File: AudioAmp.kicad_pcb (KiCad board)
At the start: 2 copper layers, 145 x 40 mm, 55 parts, among them J1 ACJS-MHOM, J2 ACJS-MHOM, Q1 MJE182G, Q12 MMBT5401, Q13 MMBT5401, Q2 MJE172G, Q3 MMBT5551(RANGE:200-300), Q9 MMBT5551(RANGE:200-300)

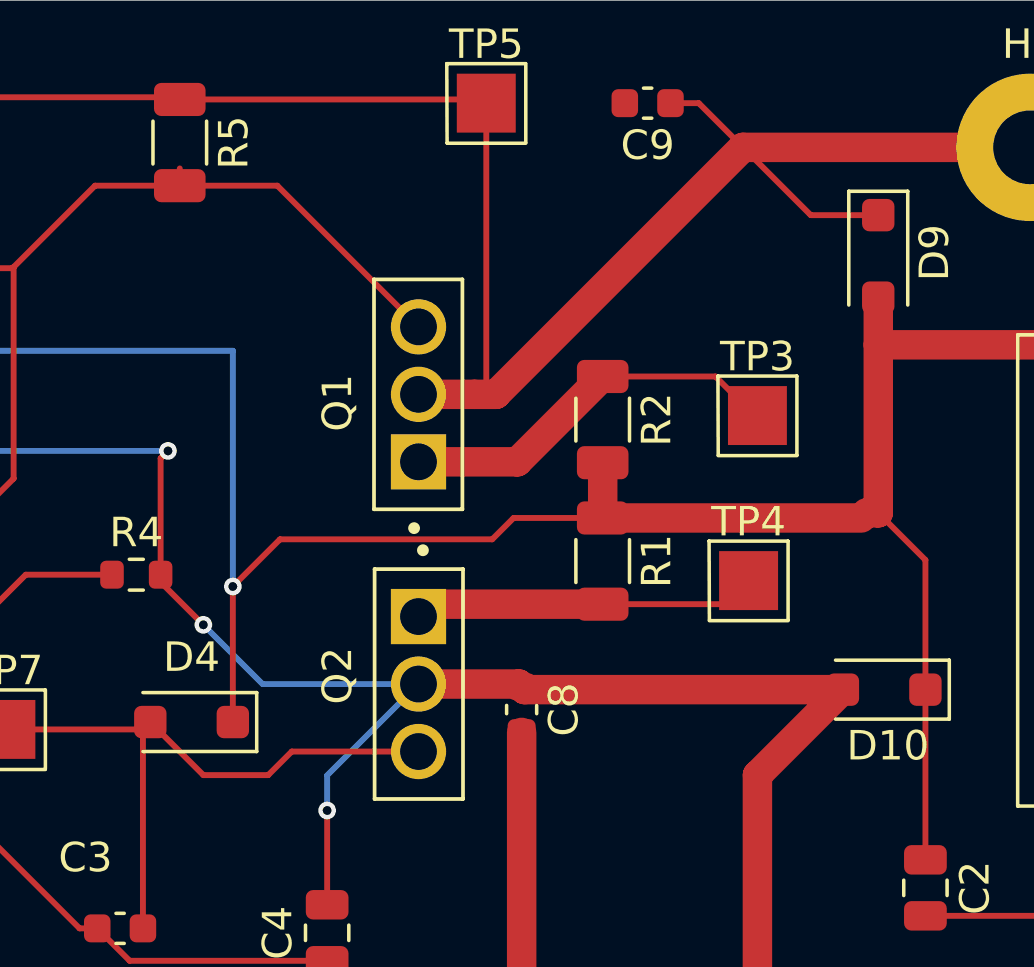
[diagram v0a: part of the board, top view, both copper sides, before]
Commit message: CHA: Insel ohne Füllung gefüllt, dazu via gesetz
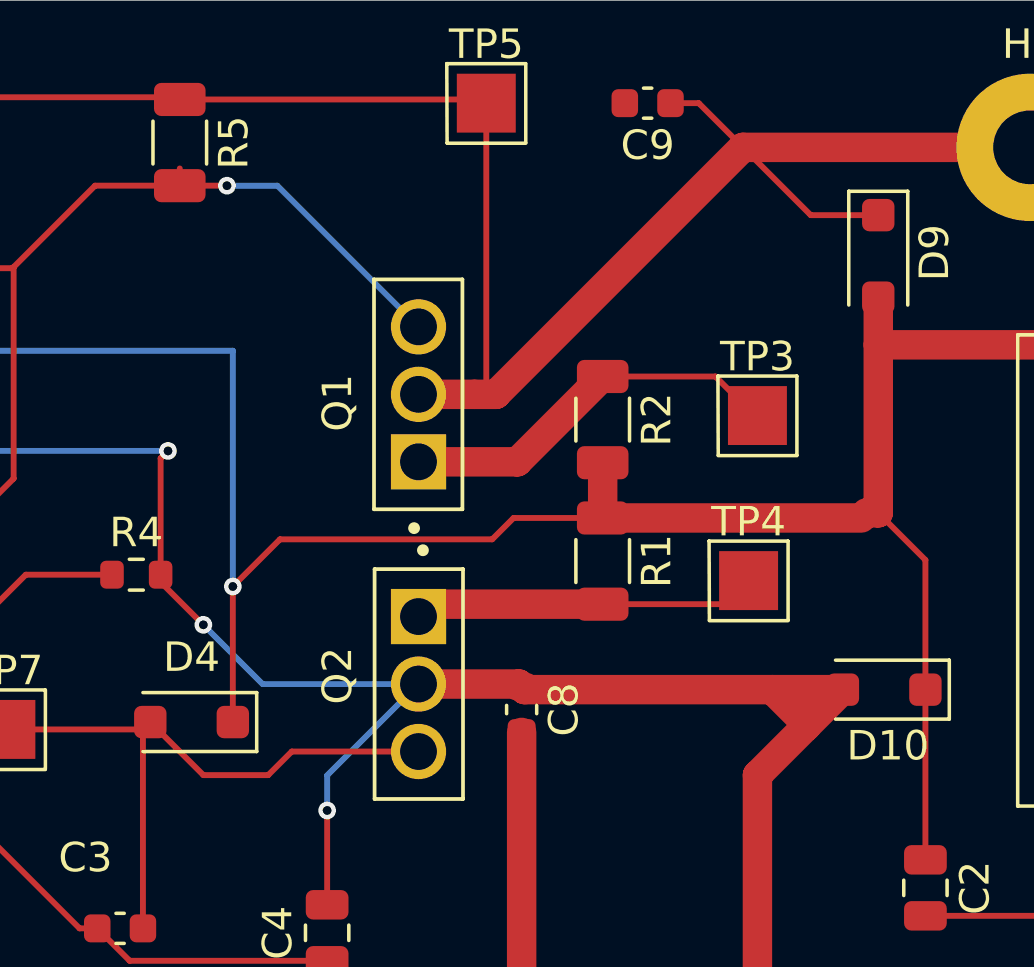
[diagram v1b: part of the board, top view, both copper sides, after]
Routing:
- net Net-(D10-A): track 90.3 -> 92.0 mm
- net Net-(D1-K): vias 0 -> 1
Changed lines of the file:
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@@
 	(segment
 		(start 168.9 110.9)
-		(end 158.1 110.9)
+		(end 166.5 110.9)
 		(width 1)
 		(layer "F.Cu")
@@
 	)
 	(segment
+		(start 166.5 110.9)
+		(end 158.1 110.9)
+		(width 1)
+		(layer "F.Cu")
+		(net 7)
+	)
+	(segment
 		(start 157.91 110.71)
 		(end 158 110.8)
@@
 	(segment
 		(start 166 113.8)
-		(end 168.9 110.9)
+		(end 167.65 112.15)
 		(width 1)
 		(layer "F.Cu")
@@
 	)
 	(segment
+		(start 167.65 112.15)
+		(end 168.9 110.9)
+		(width 1)
+		(layer "F.Cu")
+		(net 7)
+	)
+	(segment
 		(start 124 111.5)
 		(end 120.5 115)
@@
 	)
 	(segment
+		(start 167.65 112.05)
+		(end 166.5 110.9)
+		(width 1)
+		(layer "F.Cu")
+		(net 7)
+	)
+	(segment
 		(start 166.2 122.8)
 		(end 166 123)
@@
 		(start 158.1 110.9)
 		(end 158 110.8)
+		(width 1)
+		(layer "F.Cu")
+		(net 7)
+	)
+	(segment
+		(start 167.65 112.15)
+		(end 167.65 112.05)
 		(width 1)
 		(layer "F.Cu")
@@
 	)
 	(segment
+		(start 146.4 93.8)
+		(end 148 93.8)
+		(width 0.2)
+		(layer "F.Cu")
+		(net 11)
+	)
+	(segment
 		(start 137 107.5)
 		(end 140.7625 103.7375)
@@
 	)
 	(segment
+		(start 140.7625 103.7375)
+		(end 140.7625 96.5625)
+		(width 0.2)
+		(layer "F.Cu")
+		(net 11)
+	)
+	(segment
+		(start 136.9 107.6)
+		(end 137 107.5)
+		(width 0.2)
+		(layer "F.Cu")
+		(net 11)
+	)
+	(segment
+		(start 132 107.6)
+		(end 136.9 107.6)
+		(width 0.2)
+		(layer "F.Cu")
+		(net 11)
+	)
+	(via
+		(at 148 93.8)
+		(size 0.6)
+		(drill 0.3)
+		(layers "F.Cu" "B.Cu")
+		(net 11)
+	)
+	(segment
+		(start 148 93.8)
+		(end 149.71 93.8)
+		(width 0.2)
+		(layer "B.Cu")
+		(net 11)
+	)
+	(segment
 		(start 149.71 93.8)
 		(end 154.5 98.59)
 		(width 0.2)
-		(layer "F.Cu")
-		(net 11)
-	)
-	(segment
-		(start 140.7625 103.7375)
-		(end 140.7625 96.5625)
-		(width 0.2)
-		(layer "F.Cu")
-		(net 11)
-	)
-	(segment
-		(start 136.9 107.6)
-		(end 137 107.5)
-		(width 0.2)
-		(layer "F.Cu")
-		(net 11)
-	)
-	(segment
-		(start 132 107.6)
-		(end 136.9 107.6)
-		(width 0.2)
-		(layer "F.Cu")
-		(net 11)
-	)
-	(segment
-		(start 146.4 93.8)
-		(end 149.71 93.8)
-		(width 0.2)
-		(layer "F.Cu")
-		(net 11)
-	)
+		(layer "B.Cu")
+		(net 11)
+	)

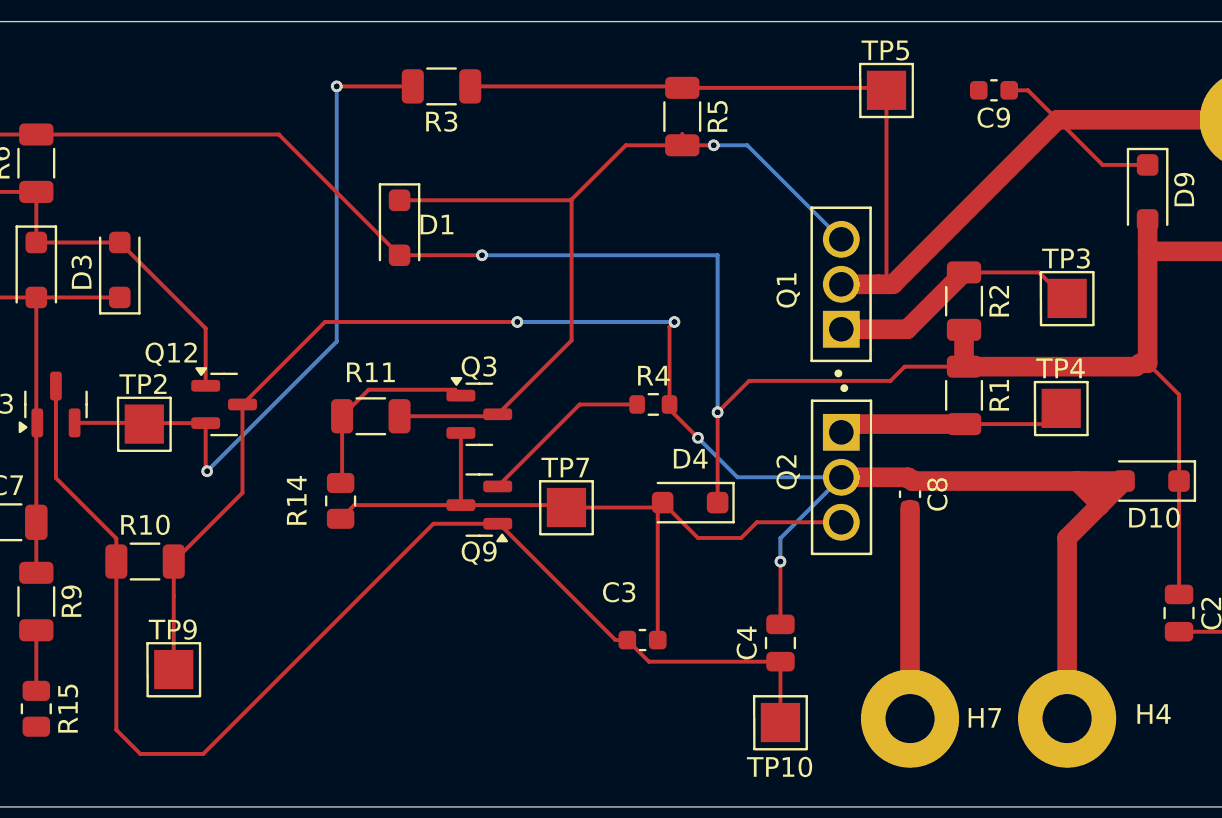
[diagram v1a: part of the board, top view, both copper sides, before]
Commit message: ^CHA: Verbesserungen Füll GND
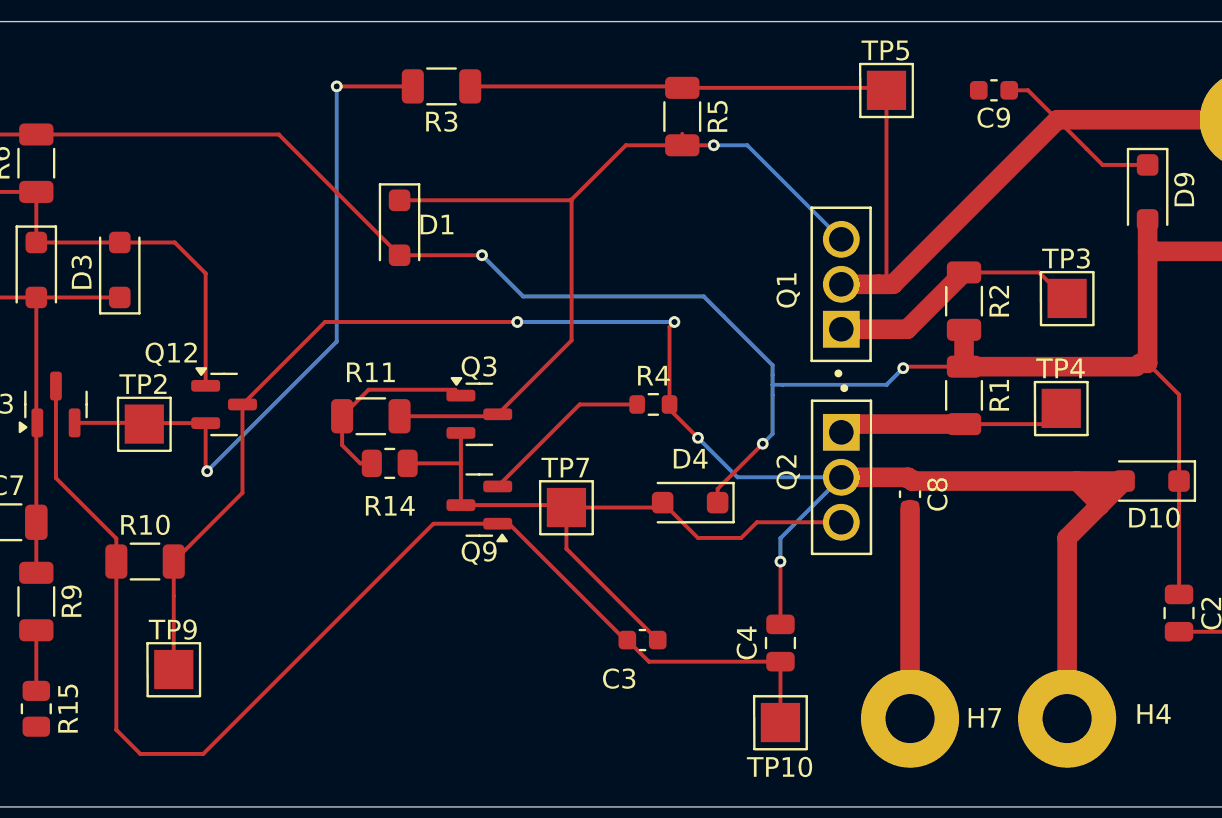
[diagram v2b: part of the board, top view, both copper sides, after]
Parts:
- moved R14 3.15 mm to (131.5, 110.0), turned to 0 degrees
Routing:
- net Net-(D1-A): track 122.8 -> 120.1 mm, vias 2 -> 3
- net Net-(D4-A): track 37.4 -> 35.7 mm
- net Net-(D2-K): track 21.0 -> 22.6 mm
